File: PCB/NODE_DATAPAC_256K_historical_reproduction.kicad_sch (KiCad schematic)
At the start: 22 parts, among them J1 Conn_02x20_Odd_Even, U1 SN74HC161N, U10 P51256SL-10, U2 SN74HC161N, U3 SN74HC161N, U4 SN74HC138N, U5 SN74HC138N, U6 74HC374N, U7 P51256SL-10, U8 P51256SL-10, U9 P51256SL-10

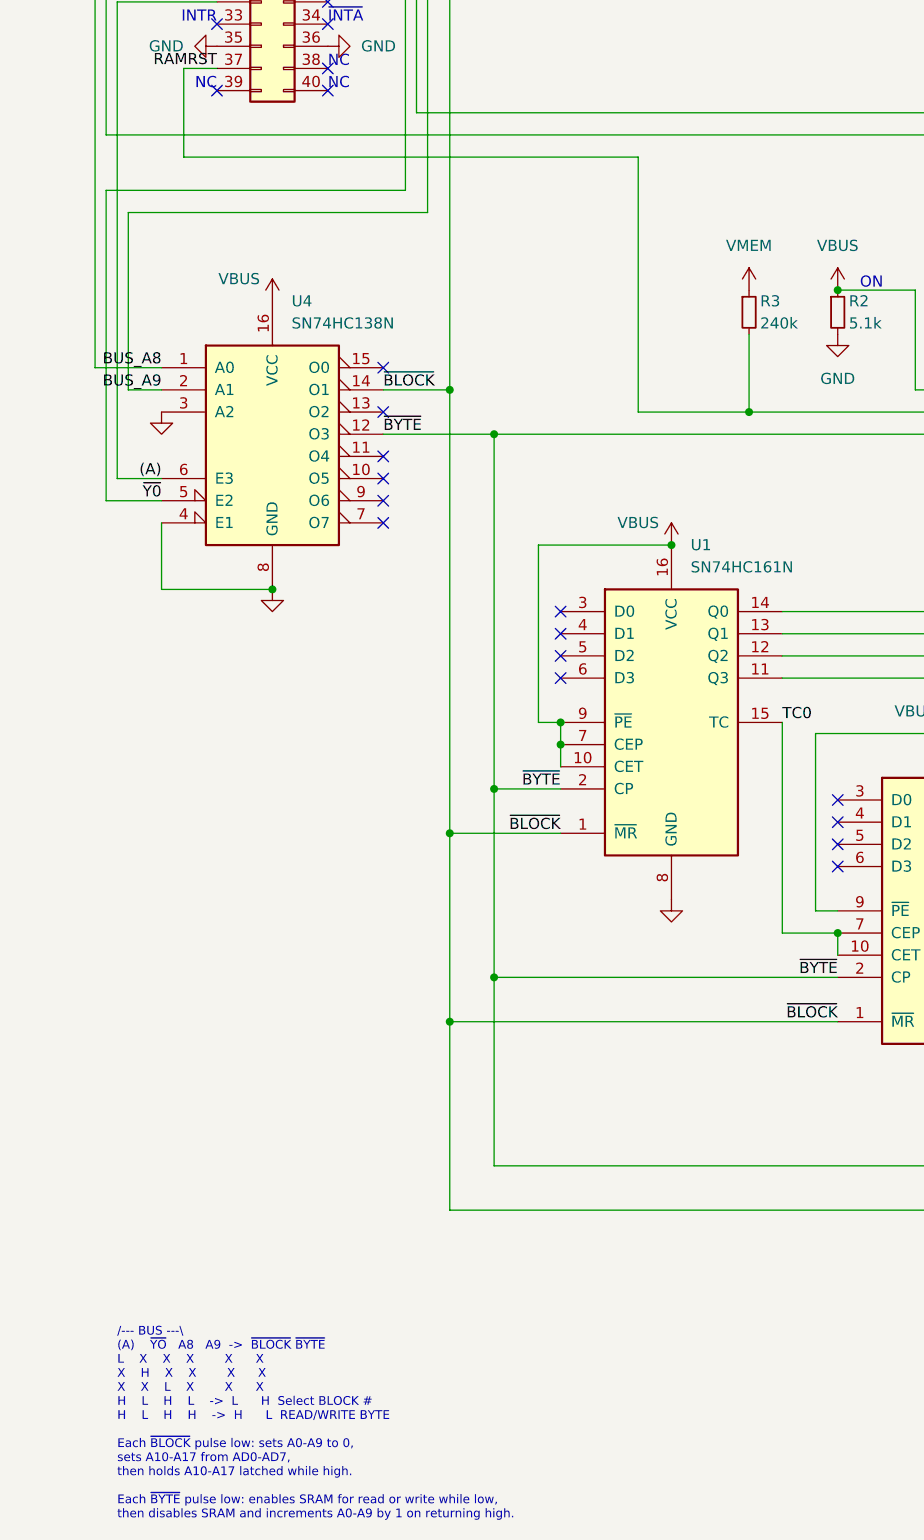
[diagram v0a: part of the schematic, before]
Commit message: notes in historical, big cap in 1M_C
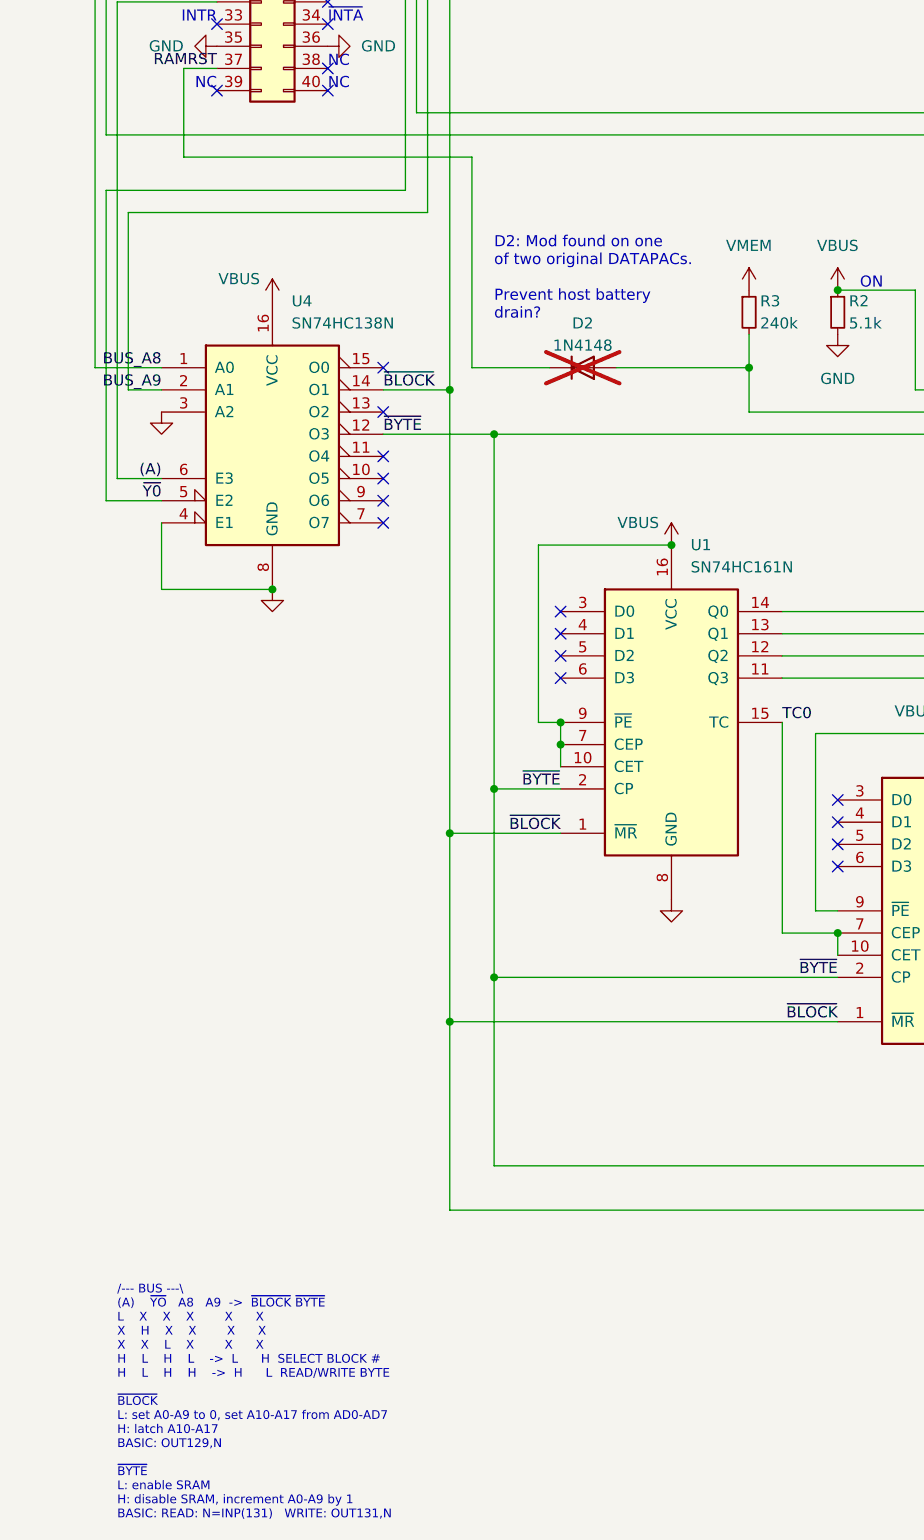
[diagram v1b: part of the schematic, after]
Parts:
- added D2: 1N4148, 000_LOCAL:D_DO-35_SOD27_P10.16mm_Horizontal, symbol 000_LOCAL:1N4148
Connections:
- net RAMRST: now also D2.1 (K), D2.2 (A)
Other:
- note added: "/--- BUS ---\ (A) ~{YO} A8 A9 -> ~{BLOCK} ~{BYTE} L X X X X X X H X X X X X X L X X X H L H L -> L H SELECT BLOCK # H L H H -> H L READ/WRITE BYTE ~{BLOCK} L: set A0-A9 to 0, set A10-A17 from AD0-AD7 H: latch A10-A17 BASIC: OUT129,N ~{BYTE} L: enable SRAM H: disable SRAM, increment A0-A9 by 1 BASIC: READ: N=INP(131) WRITE: OUT131,N"
- note added: "D2: Mod found on one of two original DATAPACs. Prevent host battery drain?"
- note removed: "/--- BUS ---\ (A) ~{YO} A8 A9 -> ~{BLOCK} ~{BYTE} L X X X X X X H X X X X X X L X X X H L H L -> L H Select BLOCK # H L H H -> H L READ/WRITE BYTE Each ~{BLOCK} pulse low: sets A0-A9 to 0, sets A10-A17 from AD0-AD7, then holds A10-A17 latched while high. Each ~{BYTE} pulse low: enables SRAM for read or write while low, then disables SRAM and increments A0-A9 by 1 on returning high."
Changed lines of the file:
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@@
 	)
 	(junction
-		(at 101.6 146.05)
-		(diameter 0)
-		(color 0 0 0 0)
-	)
-	(junction
 		(at 80.01 181.61)
 		(diameter 0)
@@
 	)
 	(junction
+		(at 101.6 140.97)
+		(diameter 0)
+		(color 0 0 0 0)
+	)
+	(junction
 		(at 236.22 31.75)
 		(diameter 0)
@@
 	(wire
 		(pts
-			(xy 36.83 116.84) (xy 88.9 116.84)
+			(xy 36.83 116.84) (xy 69.85 116.84)
 		)
 		(stroke
@@
 	(wire
 		(pts
+			(xy 86.36 140.97) (xy 101.6 140.97)
+		)
+		(stroke
+			(width 0)
+			(type default)
+		)
+	)
+	(wire
+		(pts
 			(xy 181.61 133.35) (xy 284.48 133.35)
 		)
@@
 	(wire
 		(pts
-			(xy 88.9 146.05) (xy 101.6 146.05)
+			(xy 69.85 140.97) (xy 78.74 140.97)
 		)
 		(stroke
@@
 	(wire
 		(pts
+			(xy 101.6 140.97) (xy 101.6 146.05)
+		)
+		(stroke
+			(width 0)
+			(type default)
+		)
+	)
+	(wire
+		(pts
 			(xy 228.6 111.76) (xy 228.6 88.9)
 		)
@@
 	(wire
 		(pts
-			(xy 101.6 137.16) (xy 101.6 146.05)
+			(xy 101.6 137.16) (xy 101.6 140.97)
 		)
 		(stroke
@@
 	(wire
 		(pts
-			(xy 88.9 116.84) (xy 88.9 146.05)
+			(xy 69.85 116.84) (xy 69.85 140.97)
 		)
 		(stroke
@@
 		)
 	)
+	(text "D2: Mod found on one\nof two original DATAPACs.\n\nPrevent host battery\ndrain?\n"
+		(exclude_from_sim no)
+		(at 72.39 135.636 0)
+		(effects
+			(font
+				(size 1.27 1.27)
+			)
+			(justify left bottom)
+		)
+	)
 	(text "VDD"
 		(exclude_from_sim no)
@@
 		)
 	)
-	(text "/--- BUS ---\\\n(A)	~{YO}   A8   A9  ->  ~{BLOCK} ~{BYTE}\nL	X	X	X		X	  X\nX	H	X	X		X	  X\nX	X	L	X		X	  X\nH	L	H	L	->  L	  H  Select BLOCK #\nH	L	H	H	->  H	  L  READ/WRITE BYTE\n\nEach ~{BLOCK} pulse low: sets A0-A9 to 0,\nsets A10-A17 from AD0-AD7,\nthen holds A10-A17 latched while high.\n\nEach ~{BYTE} pulse low: enables SRAM for read or write while low,\nthen disables SRAM and increments A0-A9 by 1 on returning high."
+	(text "/--- BUS ---\\\n(A)	~{YO}   A8   A9  ->  ~{BLOCK} ~{BYTE}\nL	X	X	X		X	  X\nX	H	X	X		X	  X\nX	X	L	X		X	  X\nH	L	H	L	->  L	  H  SELECT BLOCK #\nH	L	H	H	->  H	  L  READ/WRITE BYTE\n\n~{BLOCK}\nL: set A0-A9 to 0, set A10-A17 from AD0-AD7\nH: latch A10-A17\nBASIC: OUT129,N\n\n~{BYTE}\nL: enable SRAM\nH: disable SRAM, increment A0-A9 by 1\nBASIC: READ: N=INP(131)   WRITE: OUT131,N"
 		(exclude_from_sim no)
 		(at 29.21 273.05 0)
@@
 					(unit 1)
 				)
+			)
+		)
+	)
+	(symbol
+		(lib_id "000_LOCAL:1N4148")
+		(at 82.55 140.97 0)
+		(mirror x)
+		(unit 1)
+		(exclude_from_sim yes)
+		(in_bom no)
+		(on_board no)
+		(dnp yes)
+		(property "Reference" "D2"
+			(at 82.55 135.89 0)
+			(effects
+				(font
+					(size 1.27 1.27)
+				)
+			)
+		)
+		(property "Value" "1N4148"
+			(at 82.55 138.43 0)
+			(effects
+				(font
+					(size 1.27 1.27)
+				)
+			)
+		)
+		(property "Footprint" "000_LOCAL:D_DO-35_SOD27_P10.16mm_Horizontal"
+			(at 82.55 140.97 0)
+			(effects
+				(font
+					(size 1.27 1.27)
+				)
+				(hide yes)
+			)
+		)
+		(property "Datasheet" "datasheets/1N4148.pdf"
+			(at 82.55 140.97 0)
+			(effects
+				(font
+					(size 1.27 1.27)
+				)
+				(hide yes)
+			)
+		)
+		(property "Description" ""
+			(at 82.55 140.97 0)
+			(effects
+				(font
+					(size 1.27 1.27)
+				)
+				(hide yes)
+			)
+		)
+		(property "Sim.Device" "D"
+			(at 82.55 140.97 0)
+			(effects
+				(font
+					(size 1.27 1.27)
+				)
+				(hide yes)
+			)
+		)
+		(property "Sim.Pins" "1=K 2=A"
+			(at 82.55 140.97 0)
+			(effects
+				(font
+					(size 1.27 1.27)
+				)
+				(hide yes)
+			)
+		)
+		(pin "1"
+		)
+		(pin "2"
+		)
+		(instances
+			(project "NODE_DATAPAC_256K_historical_reproduction"
+				(path "/f15c2929-5cf4-4b4e-965d-148e1bec8a42"
+					(reference "D2")
+					(unit 1)
+				)

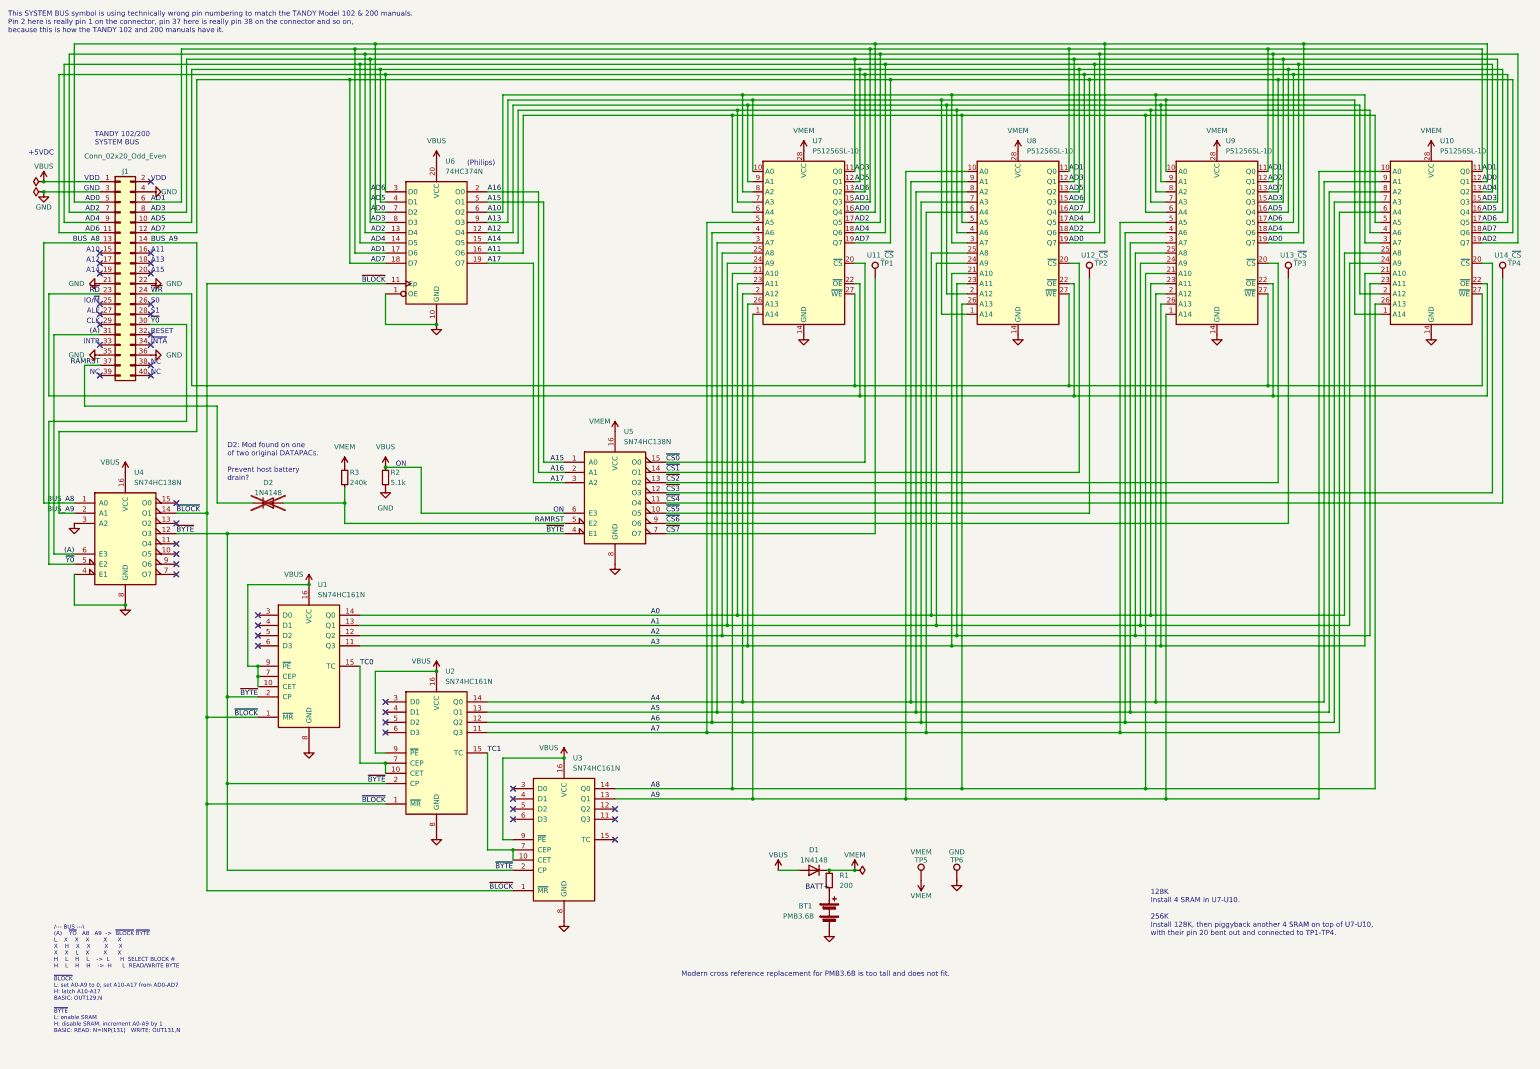
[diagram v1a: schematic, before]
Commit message: touch up notes in historical schematic
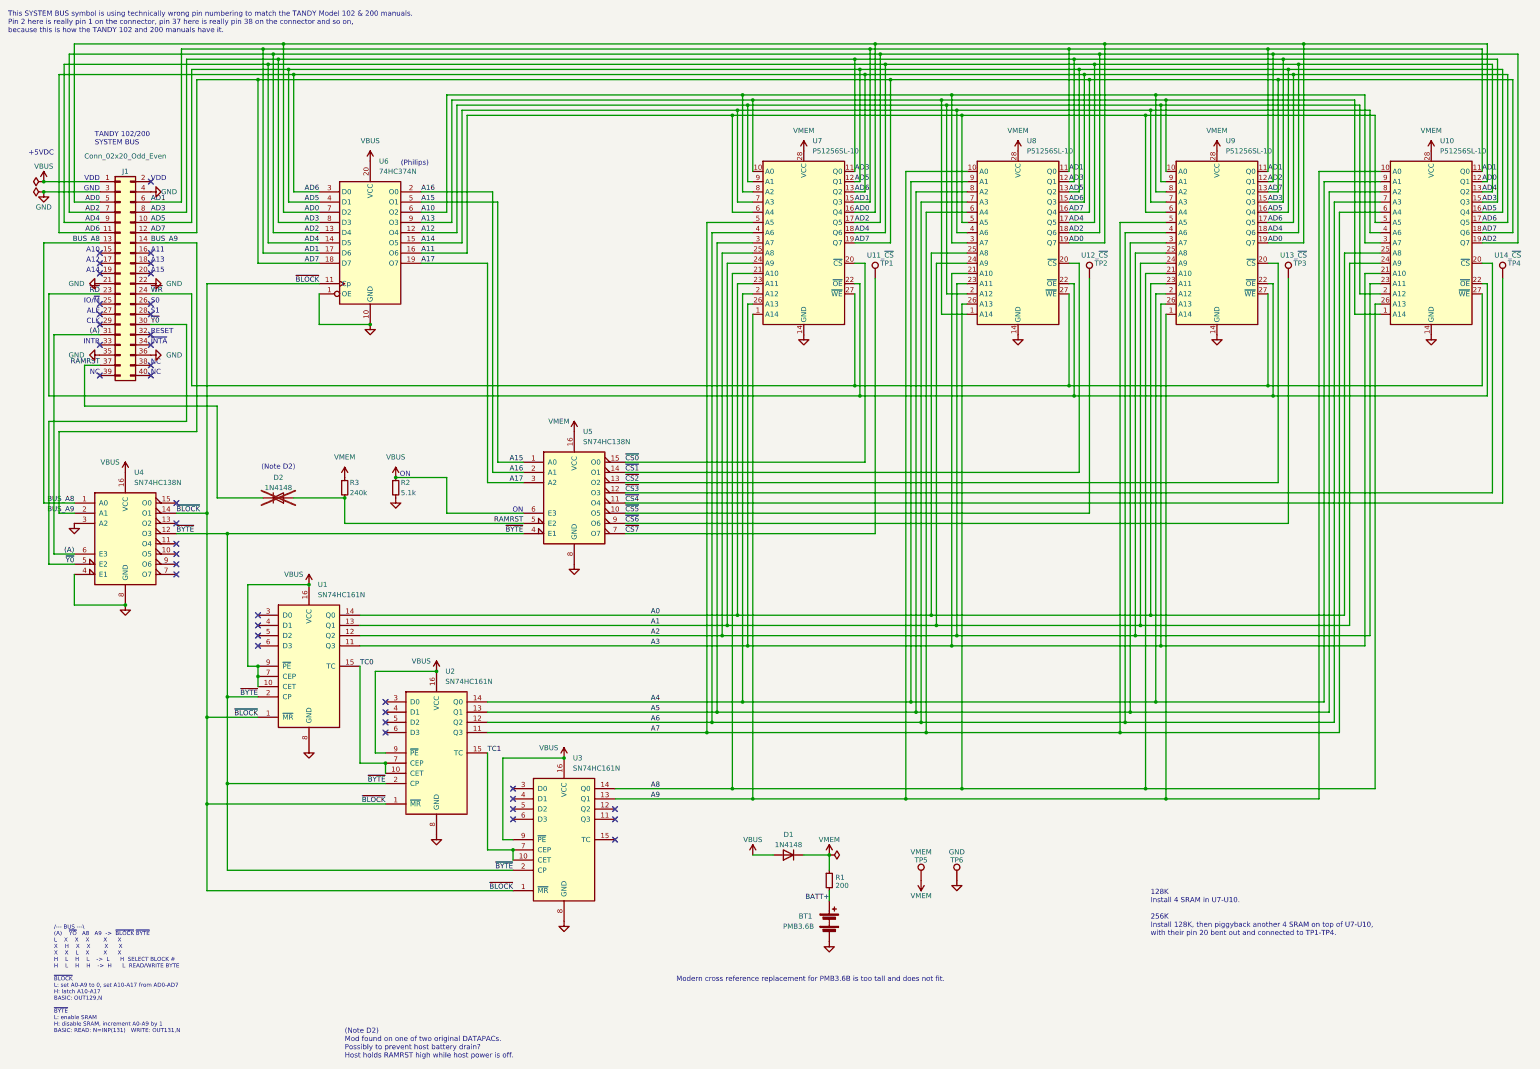
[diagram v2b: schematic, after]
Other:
- note added: "(Note D2)"
- note added: "(Note D2) Mod found on one of two original DATAPACs. Possibly to prevent host battery drain? Host holds RAMRST high while host power is off."
- note removed: "D2: Mod found on one of two original DATAPACs. Prevent host battery drain?"
- moved on the sheet: BT1, D1, D2, R2, R3, U5, U6
